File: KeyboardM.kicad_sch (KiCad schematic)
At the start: 21 parts, among them U1 ATmega32U4-A

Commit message: Annotations/ERC Run
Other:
- added sheet matrix (matrix.kicad_sch)

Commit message: Footprints Assigned
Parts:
- C1, C2, C3: renamed from C?; footprint (none) -> Capacitor_SMD:C_0805_2012Metric_Pad1.18x1.45mm_HandSolder
- C4: renamed from C1; footprint (none) -> Capacitor_SMD:C_0805_2012Metric_Pad1.18x1.45mm_HandSolder
- C5: renamed from C2; footprint (none) -> Capacitor_SMD:C_0805_2012Metric_Pad1.18x1.45mm_HandSolder
- C6: renamed from C3; footprint (none) -> Capacitor_SMD:C_0805_2012Metric_Pad1.18x1.45mm_HandSolder
- C7: renamed from C4; footprint (none) -> Capacitor_SMD:C_0805_2012Metric_Pad1.18x1.45mm_HandSolder
- C8: renamed from C5; footprint (none) -> Capacitor_SMD:C_0805_2012Metric_Pad1.18x1.45mm_HandSolder
- F1: renamed from F?; footprint (none) -> Fuse:Fuse_1206_3216Metric_Pad1.42x1.75mm_HandSolder
- J1: renamed from J?; footprint (none) -> random-keyboard-parts:Reset_Pretty-Mask
- R1, R2, R3, R4, R5, R6: renamed from R?; footprint (none) -> MX_Only:MXOnly-1U
- SW66: renamed from SW?; footprint (none) -> Button_Switch_SMD:SW_SPST_SKQG_WithStem
- U2: renamed from U?; footprint (none) -> random-keyboard-parts:SOT143B
- USB1: renamed from USB?; footprint (none) -> Type-C:HRO-TYPE-C-31-M-12-HandSoldering
- Y1: renamed from Y?; footprint (none) -> Crystal:Crystal_SMD_3225-4Pin_3.2x2.5mm_HandSoldering
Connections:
- net row0: now reaches U1.1 (PE6)
- net col8: now reaches U1.19 (PD1)
- net col9: now reaches U1.20 (PD2)
- net col10: now reaches U1.21 (PD3)
- net col11: now reaches U1.22 (PD5)
- net col12: now reaches U1.25 (PD4)
- net col13: now reaches U1.26 (PD6)
- net col14: now reaches U1.27 (PD7)
- net col0: now reaches U1.28 (PB4)
- net col1: now reaches U1.29 (PB5)
- net col2: now reaches U1.30 (PB6)
- net col3: now reaches U1.31 (PC6)
- net col4: now reaches U1.32 (PC7)
- net col6: now reaches U1.36 (PF7)
- net col5: now reaches U1.37 (PF6)
- net row1: now reaches U1.38 (PF5)
- net row4: now reaches U1.39 (PF4)
- net row3: now reaches U1.40 (PF1)
- net row2: now reaches U1.41 (PF0)
- net col7: now reaches U1.8 (PB0)
- no-connect marks 6 -> 7

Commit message: Part 2 Complete
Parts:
- removed SW66: SW_Push_Reset, Button_Switch_SMD:SW_SPST_SKQG_WithStem, symbol SW_SK:SW_SKQG
- added RSW1: SW_PUSH_RESET, Button_Switch_SMD:SW_SPST_SKQG_WithStem, symbol SW_SK:SW_SKQG
- R1, R2, R3, R4, R5, R6: footprint MX_Only:MXOnly-1U -> Resistor_SMD:R_0805_2012Metric_Pad1.20x1.40mm_HandSolder
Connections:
- net GND: now also RSW1.2
- net RESET: now also RSW1.1
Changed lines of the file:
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@@
   (no_connect (at 128.27 82.55))
   (no_connect (at 39.37 153.67))
+  (no_connect (at 49.53 109.22))
   (no_connect (at 158.75 97.79))
-  (no_connect (at 49.53 109.22))
+  (no_connect (at 39.37 168.91))
   (no_connect (at 69.85 119.38))
-  (no_connect (at 39.37 168.91))
   (no_connect (at 158.75 85.09))
   (wire (pts (xy 78.74 166.37) (xy 83.82 166.37))
@@
     (pin "4")
   )
+  (symbol (lib_id "SW_SK:SW_SKQG") (at 59.69 114.3 0) (unit 1)
+    (in_bom yes) (on_board yes) (fields_autoplaced)
+    (property "Reference" "RSW1" (id 0) (at 59.69 102.87 0))
+    (property "Value" "SW_PUSH_RESET" (id 1) (at 59.69 105.41 0))
+    (property "Footprint" "Button_Switch_SMD:SW_SPST_SKQG_WithStem" (id 2) (at 59.69 114.3 0)
+      (effects (font (size 1.27 1.27)) hide)
+    )
+    (property "Datasheet" "" (id 3) (at 59.69 114.3 0)
+      (effects (font (size 1.27 1.27)) hide)
+    )
+    (pin "1")
+    (pin "1")
+    (pin "2")
+    (pin "2")
+  )
   (symbol (lib_id "power:GND") (at 181.61 120.65 0) (unit 1)
     (in_bom yes) (on_board yes) (fields_autoplaced)
@@
     (property "Reference" "R2" (id 0) (at 170.18 114.3 90))
     (property "Value" "10k" (id 1) (at 170.18 116.84 90))
-    (property "Footprint" "MX_Only:MXOnly-1U" (id 2) (at 170.18 120.65 0)
+    (property "Footprint" "Resistor_SMD:R_0805_2012Metric_Pad1.20x1.40mm_HandSolder" (id 2) (at 170.18 120.65 0)
       (effects (font (size 1.27 1.27)) hide)
     )
@@
     (pin "1")
     (pin "2")
-  )
-  (symbol (lib_id "SW_SK:SW_SKQG") (at 59.69 114.3 0) (unit 1)
-    (in_bom yes) (on_board yes)
-    (property "Reference" "SW66" (id 0) (at 59.69 101.6 0))
-    (property "Value" "SW_Push_Reset" (id 1) (at 59.69 104.14 0))
-    (property "Footprint" "Button_Switch_SMD:SW_SPST_SKQG_WithStem" (id 2) (at 59.69 114.3 0)
-      (effects (font (size 1.27 1.27)) hide)
-    )
-    (property "Datasheet" "" (id 3) (at 59.69 114.3 0)
-      (effects (font (size 1.27 1.27)) hide)
-    )
-    (pin "")
-    (pin "")
-    (pin "")
-    (pin "")
   )
   (symbol (lib_id "power:GND") (at 130.81 156.21 0) (unit 1)
@@
     (property "Reference" "R4" (id 0) (at 86.36 171.45 90))
     (property "Value" "22" (id 1) (at 86.36 168.91 90))
-    (property "Footprint" "MX_Only:MXOnly-1U" (id 2) (at 86.36 166.37 0)
+    (property "Footprint" "Resistor_SMD:R_0805_2012Metric_Pad1.20x1.40mm_HandSolder" (id 2) (at 86.36 166.37 0)
       (effects (font (size 1.27 1.27)) hide)
     )
@@
       (effects (font (size 1.27 1.27)) (justify left))
     )
-    (property "Footprint" "MX_Only:MXOnly-1U" (id 2) (at 76.2 104.14 0)
+    (property "Footprint" "Resistor_SMD:R_0805_2012Metric_Pad1.20x1.40mm_HandSolder" (id 2) (at 76.2 104.14 0)
       (effects (font (size 1.27 1.27)) hide)
     )
@@
       (effects (font (size 1.27 1.27)) (justify left))
     )
-    (property "Footprint" "MX_Only:MXOnly-1U" (id 2) (at 54.61 173.99 0)
+    (property "Footprint" "Resistor_SMD:R_0805_2012Metric_Pad1.20x1.40mm_HandSolder" (id 2) (at 54.61 173.99 0)
       (effects (font (size 1.27 1.27)) hide)
     )
@@
       (effects (font (size 1.27 1.27)) (justify left))
     )
-    (property "Footprint" "MX_Only:MXOnly-1U" (id 2) (at 49.53 173.99 0)
+    (property "Footprint" "Resistor_SMD:R_0805_2012Metric_Pad1.20x1.40mm_HandSolder" (id 2) (at 49.53 173.99 0)
       (effects (font (size 1.27 1.27)) hide)
     )
@@
     (property "Reference" "R3" (id 0) (at 86.36 158.75 90))
     (property "Value" "22" (id 1) (at 86.36 161.29 90))
-    (property "Footprint" "MX_Only:MXOnly-1U" (id 2) (at 86.36 163.83 0)
+    (property "Footprint" "Resistor_SMD:R_0805_2012Metric_Pad1.20x1.40mm_HandSolder" (id 2) (at 86.36 163.83 0)
       (effects (font (size 1.27 1.27)) hide)
     )
@@
     (pin "4")
   )
-  (sheet (at 212.09 87.63) (size 12.7 3.81) (fields_autoplaced)
+  (sheet (at 175.26 93.98) (size 12.7 3.81) (fields_autoplaced)
     (stroke (width 0.1524) (type solid) (color 0 0 0 0))
     (fill (color 0 0 0 0.0000))
-    (property "Sheet name" "matrix" (id 0) (at 212.09 86.9184 0)
+    (property "Sheet name" "matrix" (id 0) (at 175.26 93.2684 0)
       (effects (font (size 1.27 1.27)) (justify left bottom))
     )
-    (property "Sheet file" "matrix.kicad_sch" (id 1) (at 212.09 92.0246 0)
+    (property "Sheet file" "matrix.kicad_sch" (id 1) (at 175.26 98.3746 0)
       (effects (font (size 1.27 1.27)) (justify left top))
     )
@@
     )
     (path "/3765e45a-9f1d-4cae-805e-320f859ddcac"
-      (reference "R1") (unit 1) (value "10k") (footprint "MX_Only:MXOnly-1U")
+      (reference "R1") (unit 1) (value "10k") (footprint "Resistor_SMD:R_0805_2012Metric_Pad1.20x1.40mm_HandSolder")
     )
     (path "/1a8a98e6-ae33-4f50-94b6-5a8676312783"
-      (reference "R2") (unit 1) (value "10k") (footprint "MX_Only:MXOnly-1U")
+      (reference "R2") (unit 1) (value "10k") (footprint "Resistor_SMD:R_0805_2012Metric_Pad1.20x1.40mm_HandSolder")
     )
     (path "/dbe96627-6a09-447b-9415-6200b9308ca6"
-      (reference "R3") (unit 1) (value "22") (footprint "MX_Only:MXOnly-1U")
+      (reference "R3") (unit 1) (value "22") (footprint "Resistor_SMD:R_0805_2012Metric_Pad1.20x1.40mm_HandSolder")
     )
     (path "/2bf873e5-6490-4304-a3be-d5a53e47faad"
-      (reference "R4") (unit 1) (value "22") (footprint "MX_Only:MXOnly-1U")
+      (reference "R4") (unit 1) (value "22") (footprint "Resistor_SMD:R_0805_2012Metric_Pad1.20x1.40mm_HandSolder")
     )
     (path "/cfe53b80-e710-4c04-a03d-4e757032eb32"
-      (reference "R5") (unit 1) (value "5.1k") (footprint "MX_Only:MXOnly-1U")
+      (reference "R5") (unit 1) (value "5.1k") (footprint "Resistor_SMD:R_0805_2012Metric_Pad1.20x1.40mm_HandSolder")
     )
     (path "/65f3a5ff-1c48-407a-af85-12a56aa59f33"
-      (reference "R6") (unit 1) (value "5.1k") (footprint "MX_Only:MXOnly-1U")
+      (reference "R6") (unit 1) (value "5.1k") (footprint "Resistor_SMD:R_0805_2012Metric_Pad1.20x1.40mm_HandSolder")
+    )
+    (path "/0532b1bb-89cb-461c-ac2e-8086df8ac37a"
+      (reference "RSW1") (unit 1) (value "SW_PUSH_RESET") (footprint "Button_Switch_SMD:SW_SPST_SKQG_WithStem")
     )
     (path "/71755621-1f0d-4bdb-b18c-9e331608c358/a6e4c1e6-1dec-4bd2-95d9-75a756a4ca87"
@@
       (reference "SW65") (unit 1) (value "RIGHT") (footprint "MX_Only:MXOnly-1U")
     )
-    (path "/1e9d23fa-be3c-4e69-a344-cab8d50a31e5"
-      (reference "SW66") (unit 1) (value "SW_Push_Reset") (footprint "Button_Switch_SMD:SW_SPST_SKQG_WithStem")
-    )
     (path "/b83167fd-d647-4e90-9efb-cea133c4b82f"

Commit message: Wiring
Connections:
- net DP: now reaches R4.1, U2.2 (IO1), USB1.6 (DP1), USB1.8 (DP2)
- net DP: no longer USB1.5 (DN2)
- net DN: now reaches R3.1, U2.3 (IO2), USB1.7 (DN1)
- net DN: now also USB1.5 (DN2)
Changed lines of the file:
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@@
   (junction (at 95.25 81.28) (diameter 0) (color 0 0 0 0)
   )
-  (junction (at 49.53 166.37) (diameter 0) (color 0 0 0 0)
-  )
   (junction (at 95.25 83.82) (diameter 0) (color 0 0 0 0)
+  )
+  (junction (at 49.53 163.83) (diameter 0) (color 0 0 0 0)
   )
   (junction (at 76.2 109.22) (diameter 0) (color 0 0 0 0)
@@
     (stroke (width 0) (type default) (color 0 0 0 0))
   )
-  (wire (pts (xy 46.99 166.37) (xy 49.53 166.37))
-    (stroke (width 0) (type default) (color 0 0 0 0))
-  )
   (wire (pts (xy 49.53 176.53) (xy 54.61 176.53))
     (stroke (width 0) (type default) (color 0 0 0 0))
@@
     (stroke (width 0) (type default) (color 0 0 0 0))
   )
+  (wire (pts (xy 49.53 163.83) (xy 60.96 163.83))
+    (stroke (width 0) (type default) (color 0 0 0 0))
+  )
   (wire (pts (xy 87.63 83.82) (xy 95.25 83.82))
     (stroke (width 0) (type default) (color 0 0 0 0))
@@
     (stroke (width 0) (type default) (color 0 0 0 0))
   )
+  (wire (pts (xy 100.33 72.39) (xy 100.33 81.28))
+    (stroke (width 0) (type default) (color 0 0 0 0))
+  )
+  (wire (pts (xy 69.85 109.22) (xy 76.2 109.22))
+    (stroke (width 0) (type default) (color 0 0 0 0))
+  )
+  (wire (pts (xy 44.45 176.53) (xy 44.45 181.61))
+    (stroke (width 0) (type default) (color 0 0 0 0))
+  )
+  (wire (pts (xy 107.95 135.89) (xy 113.03 135.89))
+    (stroke (width 0) (type default) (color 0 0 0 0))
+  )
+  (wire (pts (xy 88.9 166.37) (xy 92.71 166.37))
+    (stroke (width 0) (type default) (color 0 0 0 0))
+  )
+  (wire (pts (xy 172.72 120.65) (xy 181.61 120.65))
+    (stroke (width 0) (type default) (color 0 0 0 0))
+  )
+  (wire (pts (xy 46.99 166.37) (xy 78.74 166.37))
+    (stroke (width 0) (type default) (color 0 0 0 0))
+  )
+  (wire (pts (xy 39.37 161.29) (xy 46.99 161.29))
+    (stroke (width 0) (type default) (color 0 0 0 0))
+  )
+  (wire (pts (xy 46.99 119.38) (xy 46.99 121.92))
+    (stroke (width 0) (type default) (color 0 0 0 0))
+  )
+  (wire (pts (xy 87.63 81.28) (xy 87.63 83.82))
+    (stroke (width 0) (type default) (color 0 0 0 0))
+  )
+  (wire (pts (xy 54.61 156.21) (xy 39.37 156.21))
+    (stroke (width 0) (type default) (color 0 0 0 0))
+  )
+  (wire (pts (xy 39.37 171.45) (xy 49.53 171.45))
+    (stroke (width 0) (type default) (color 0 0 0 0))
+  )
+  (wire (pts (xy 143.51 151.13) (xy 140.97 151.13))
+    (stroke (width 0) (type default) (color 0 0 0 0))
+  )
+  (wire (pts (xy 140.97 151.13) (xy 130.81 151.13))
+    (stroke (width 0) (type default) (color 0 0 0 0))
+  )
+  (wire (pts (xy 76.2 106.68) (xy 76.2 109.22))
+    (stroke (width 0) (type default) (color 0 0 0 0))
+  )
+  (wire (pts (xy 48.26 151.13) (xy 53.34 151.13))
+    (stroke (width 0) (type default) (color 0 0 0 0))
+  )
+  (wire (pts (xy 53.34 151.13) (xy 57.15 151.13))
+    (stroke (width 0) (type default) (color 0 0 0 0))
+  )
+  (wire (pts (xy 100.33 81.28) (xy 95.25 81.28))
+    (stroke (width 0) (type default) (color 0 0 0 0))
+  )
   (wire (pts (xy 39.37 158.75) (xy 49.53 158.75))
     (stroke (width 0) (type default) (color 0 0 0 0))
   )
-  (wire (pts (xy 100.33 72.39) (xy 100.33 81.28))
-    (stroke (width 0) (type default) (color 0 0 0 0))
-  )
-  (wire (pts (xy 69.85 109.22) (xy 76.2 109.22))
-    (stroke (width 0) (type default) (color 0 0 0 0))
-  )
-  (wire (pts (xy 44.45 176.53) (xy 44.45 181.61))
-    (stroke (width 0) (type default) (color 0 0 0 0))
-  )
-  (wire (pts (xy 107.95 135.89) (xy 113.03 135.89))
-    (stroke (width 0) (type default) (color 0 0 0 0))
-  )
-  (wire (pts (xy 88.9 166.37) (xy 92.71 166.37))
-    (stroke (width 0) (type default) (color 0 0 0 0))
-  )
-  (wire (pts (xy 172.72 120.65) (xy 181.61 120.65))
-    (stroke (width 0) (type default) (color 0 0 0 0))
-  )
-  (wire (pts (xy 49.53 166.37) (xy 78.74 166.37))
-    (stroke (width 0) (type default) (color 0 0 0 0))
-  )
-  (wire (pts (xy 39.37 161.29) (xy 46.99 161.29))
-    (stroke (width 0) (type default) (color 0 0 0 0))
-  )
-  (wire (pts (xy 46.99 119.38) (xy 46.99 121.92))
-    (stroke (width 0) (type default) (color 0 0 0 0))
-  )
-  (wire (pts (xy 87.63 81.28) (xy 87.63 83.82))
-    (stroke (width 0) (type default) (color 0 0 0 0))
-  )
-  (wire (pts (xy 54.61 156.21) (xy 39.37 156.21))
-    (stroke (width 0) (type default) (color 0 0 0 0))
-  )
-  (wire (pts (xy 49.53 158.75) (xy 49.53 166.37))
-    (stroke (width 0) (type default) (color 0 0 0 0))
-  )
-  (wire (pts (xy 39.37 171.45) (xy 49.53 171.45))
-    (stroke (width 0) (type default) (color 0 0 0 0))
-  )
-  (wire (pts (xy 143.51 151.13) (xy 140.97 151.13))
-    (stroke (width 0) (type default) (color 0 0 0 0))
-  )
-  (wire (pts (xy 140.97 151.13) (xy 130.81 151.13))
-    (stroke (width 0) (type default) (color 0 0 0 0))
-  )
-  (wire (pts (xy 76.2 106.68) (xy 76.2 109.22))
-    (stroke (width 0) (type default) (color 0 0 0 0))
-  )
-  (wire (pts (xy 48.26 151.13) (xy 53.34 151.13))
-    (stroke (width 0) (type default) (color 0 0 0 0))
-  )
-  (wire (pts (xy 53.34 151.13) (xy 57.15 151.13))
-    (stroke (width 0) (type default) (color 0 0 0 0))
-  )
-  (wire (pts (xy 100.33 81.28) (xy 95.25 81.28))
-    (stroke (width 0) (type default) (color 0 0 0 0))
-  )
   (wire (pts (xy 113.03 135.89) (xy 118.11 135.89))
     (stroke (width 0) (type default) (color 0 0 0 0))
@@
     (stroke (width 0) (type default) (color 0 0 0 0))
   )
+  (wire (pts (xy 49.53 158.75) (xy 49.53 163.83))
+    (stroke (width 0) (type default) (color 0 0 0 0))
+  )
   (wire (pts (xy 49.53 119.38) (xy 46.99 119.38))
     (stroke (width 0) (type default) (color 0 0 0 0))
@@
     (stroke (width 0) (type default) (color 0 0 0 0))
   )
-  (wire (pts (xy 39.37 163.83) (xy 60.96 163.83))
+  (wire (pts (xy 39.37 163.83) (xy 49.53 163.83))
     (stroke (width 0) (type default) (color 0 0 0 0))
   )
@@
     (stroke (width 0) (type default) (color 0 0 0 0))
   )
+  (global_label "DN" (shape input) (at 57.404 163.83 90) (fields_autoplaced)
+    (effects (font (size 1.27 1.27)) (justify left))
+    (property "Intersheet References" "${INTERSHEET_REFS}" (id 0) (at 57.3246 158.8164 90)
+      (effects (font (size 1.27 1.27)) (justify left) hide)
+    )
+  )
   (global_label "row4" (shape input) (at 158.75 133.35 0) (fields_autoplaced)
     (effects (font (size 1.27 1.27)) (justify left))
@@
     )
   )
+  (global_label "DP" (shape input) (at 57.404 166.37 270) (fields_autoplaced)
+    (effects (font (size 1.27 1.27)) (justify right))
+    (property "Intersheet References" "${INTERSHEET_REFS}" (id 0) (at 57.3246 171.3231 90)
+      (effects (font (size 1.27 1.27)) (justify right) hide)
+    )
+  )

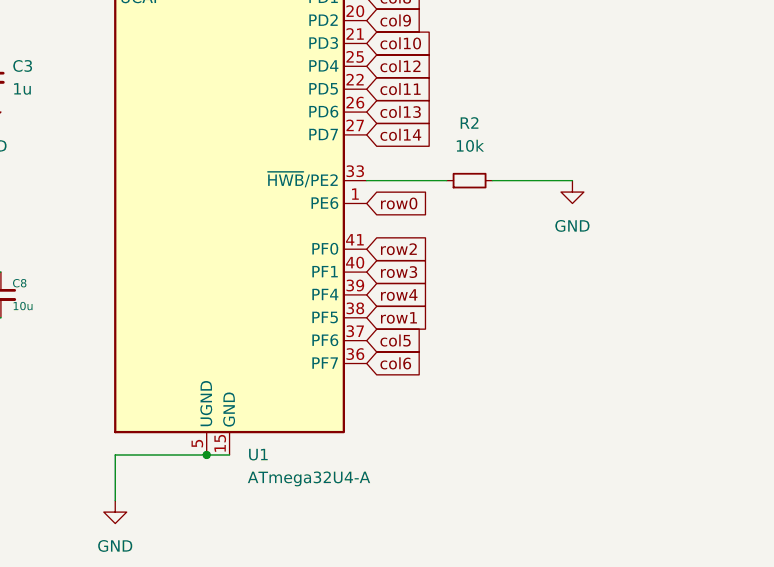
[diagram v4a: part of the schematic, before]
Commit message: Routing Complete
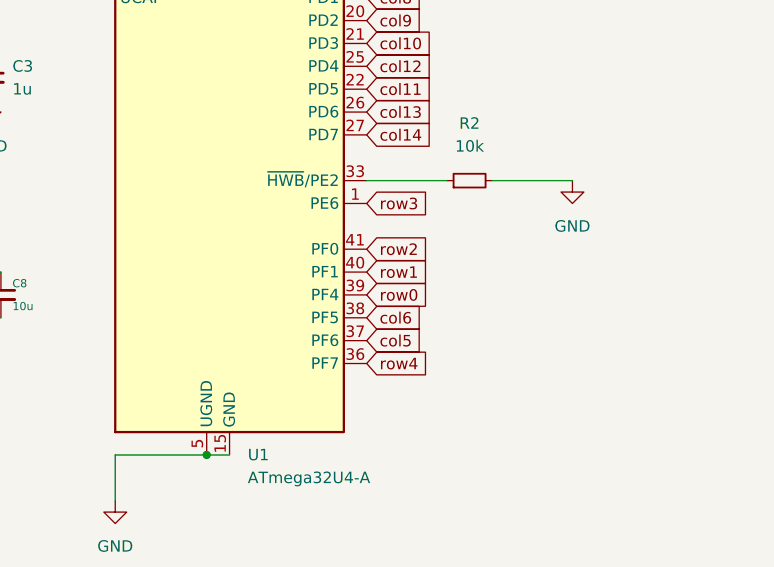
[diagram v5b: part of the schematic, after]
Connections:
- net col6: now also U1.38 (PF5); no longer U1.36 (PF7)
- net row0: now also U1.39 (PF4); no longer U1.1 (PE6)
- net row1: now also U1.40 (PF1); no longer U1.38 (PF5)
- net row3: now also U1.1 (PE6); no longer U1.40 (PF1)
- net row4: now also U1.36 (PF7); no longer U1.39 (PF4)
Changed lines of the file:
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@@
     )
   )
-  (global_label "row4" (shape input) (at 158.75 133.35 0) (fields_autoplaced)
-    (effects (font (size 1.27 1.27)) (justify left))
-    (property "Intersheet References" "${INTERSHEET_REFS}" (id 0) (at 165.6383 133.2706 0)
+  (global_label "row4" (shape input) (at 158.75 140.97 0) (fields_autoplaced)
+    (effects (font (size 1.27 1.27)) (justify left))
+    (property "Intersheet References" "${INTERSHEET_REFS}" (id 0) (at 165.6383 140.8906 0)
       (effects (font (size 1.27 1.27)) (justify left) hide)
     )
@@
     )
   )
-  (global_label "col6" (shape input) (at 158.75 140.97 0) (fields_autoplaced)
-    (effects (font (size 1.27 1.27)) (justify left))
-    (property "Intersheet References" "${INTERSHEET_REFS}" (id 0) (at 165.2755 140.8906 0)
+  (global_label "col6" (shape input) (at 158.75 135.89 0) (fields_autoplaced)
+    (effects (font (size 1.27 1.27)) (justify left))
+    (property "Intersheet References" "${INTERSHEET_REFS}" (id 0) (at 165.2755 135.8106 0)
       (effects (font (size 1.27 1.27)) (justify left) hide)
     )
@@
     )
   )
-  (global_label "row3" (shape input) (at 158.75 130.81 0) (fields_autoplaced)
-    (effects (font (size 1.27 1.27)) (justify left))
-    (property "Intersheet References" "${INTERSHEET_REFS}" (id 0) (at 165.6383 130.7306 0)
+  (global_label "row3" (shape input) (at 158.75 123.19 0) (fields_autoplaced)
+    (effects (font (size 1.27 1.27)) (justify left))
+    (property "Intersheet References" "${INTERSHEET_REFS}" (id 0) (at 165.6383 123.1106 0)
       (effects (font (size 1.27 1.27)) (justify left) hide)
     )
@@
     )
   )
-  (global_label "row0" (shape input) (at 158.75 123.19 0) (fields_autoplaced)
-    (effects (font (size 1.27 1.27)) (justify left))
-    (property "Intersheet References" "${INTERSHEET_REFS}" (id 0) (at 165.6383 123.1106 0)
+  (global_label "row0" (shape input) (at 158.75 133.35 0) (fields_autoplaced)
+    (effects (font (size 1.27 1.27)) (justify left))
+    (property "Intersheet References" "${INTERSHEET_REFS}" (id 0) (at 165.6383 133.2706 0)
       (effects (font (size 1.27 1.27)) (justify left) hide)
     )
@@
     )
   )
-  (global_label "row1" (shape input) (at 158.75 135.89 0) (fields_autoplaced)
-    (effects (font (size 1.27 1.27)) (justify left))
-    (property "Intersheet References" "${INTERSHEET_REFS}" (id 0) (at 165.6383 135.8106 0)
+  (global_label "row1" (shape input) (at 158.75 130.81 0) (fields_autoplaced)
+    (effects (font (size 1.27 1.27)) (justify left))
+    (property "Intersheet References" "${INTERSHEET_REFS}" (id 0) (at 165.6383 130.7306 0)
       (effects (font (size 1.27 1.27)) (justify left) hide)
     )
@@
     )
     (path "/71755621-1f0d-4bdb-b18c-9e331608c358/a6e4c1e6-1dec-4bd2-95d9-75a756a4ca87"
-      (reference "SW1") (unit 1) (value "`") (footprint "MX_Only:MXOnly-1U")
+      (reference "SW1") (unit 1) (value "`~") (footprint "MX_Only:MXOnly-1U")
     )
     (path "/71755621-1f0d-4bdb-b18c-9e331608c358/c49ef9ba-14c0-477d-8c4e-bffae8c73d8a"
@@
     )
     (path "/71755621-1f0d-4bdb-b18c-9e331608c358/94844779-02e2-4f81-9129-4ca12f98cc41"
-      (reference "SW12") (unit 1) (value "-") (footprint "MX_Only:MXOnly-1U")
+      (reference "SW12") (unit 1) (value "-_") (footprint "MX_Only:MXOnly-1U")
     )
     (path "/71755621-1f0d-4bdb-b18c-9e331608c358/811a003a-62ea-4da6-83e7-95a4378fd47c"
-      (reference "SW13") (unit 1) (value "=") (footprint "MX_Only:MXOnly-1U")
+      (reference "SW13") (unit 1) (value "=+") (footprint "MX_Only:MXOnly-1U")
     )
     (path "/71755621-1f0d-4bdb-b18c-9e331608c358/ba173afe-5e65-47fe-bb8b-e1a7315d8545"
@@
     )
     (path "/71755621-1f0d-4bdb-b18c-9e331608c358/b5e525de-5ce3-4199-a0a6-b3b56fc56458"
-      (reference "SW60") (unit 1) (value "SPACE") (footprint "MX_Only:MXOnly-6.25U")
+      (reference "SW60") (unit 1) (value "SPACE") (footprint "MX_Only:MXOnly-6.25U-ReversedStabilizers")
     )
     (path "/71755621-1f0d-4bdb-b18c-9e331608c358/e5ffb86f-0639-4a1d-a04b-348d1932a7da"

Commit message: v1.0.0
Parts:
- added FB1: 60@100MHz, Inductor_SMD:L_0805_2012Metric_Pad1.15x1.40mm_HandSolder, symbol Device:FerriteBead_Small
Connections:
- net GND: now also FB1.1; no longer USB1.13 (SHIELD)
- new net Earth: FB1.2, USB1.13 (SHIELD)
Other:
- moved on the sheet: F1, R3, R4, R5, R6, U2, USB1
